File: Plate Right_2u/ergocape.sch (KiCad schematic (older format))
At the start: 42 parts

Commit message: cleanup and finish the case files
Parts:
- removed K_ESC1: KEYSW, acheron_SwitchSlots:slotMX100, symbol keyboard_parts:KEYSW
- added K_BKSP_1: KEYSW, usbc_footprint:slotMX200, symbol keyboard_parts:KEYSW
- H1, H10, H11, H12, H2, H3, H5, H6, H8, H9: footprint usbc_footprint:mount_hole_2.4x4 -> acheron_MountingHoles:MountingHole_2.5x4.0mm
- K_1, K_2, K_3, K_4, K_5, K_A1, K_ALT1, K_B1, K_BOT_1U_1, K_BOT_1U_2, K_C1, K_CTRL1, K_D1, K_E1, K_F1, K_G1, K_Q1, K_R1, K_S1, K_T1, K_TAB1, K_TH_1U_1, K_TH_1U_2, K_V1, K_W1, K_WIN1, K_X1, K_Z1: footprint acheron_SwitchSlots:slotMX100 -> usbc_footprint:slotMX100
- K_ENTER_rev_2.25u_1, K_SHIFT_REV_2.75_1, K_THUMB_2U1: footprint acheron_SwitchSlots:slotMX200 -> usbc_footprint:slotMX200
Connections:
- wire segments 5 -> 1

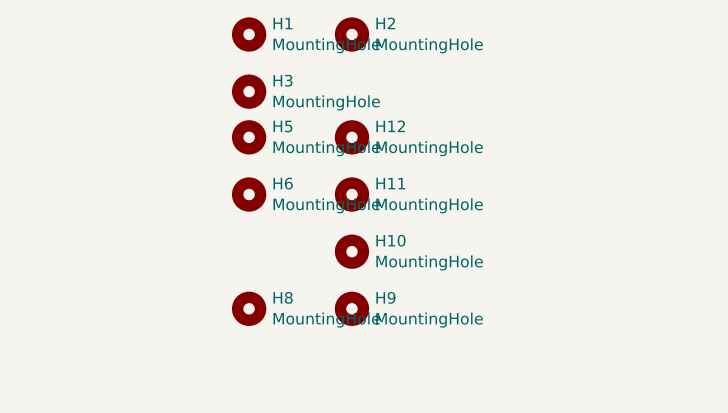
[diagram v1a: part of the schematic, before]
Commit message: finalize plate and mounting holes
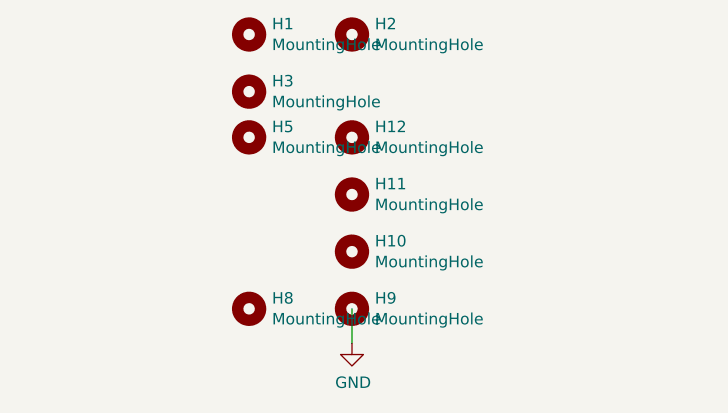
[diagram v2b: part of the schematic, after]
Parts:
- removed H6: MountingHole, acheron_MountingHoles:MountingHole_2.5x4.0mm, symbol Mechanical:MountingHole
- H1, H10, H11, H12, H2, H3, H5, H8, H9: footprint acheron_MountingHoles:MountingHole_2.5x4.0mm -> MountingHole:MountingHole_2.7mm_M2.5
- K_1, K_2, K_3, K_4, K_5, K_A1, K_ALT1, K_B1, K_BOT_1U_1, K_BOT_1U_2, K_C1, K_CTRL1, K_D1, K_E1, K_F1, K_G1, K_Q1, K_R1, K_S1, K_T1, K_TAB1, K_TH_1U_1, K_TH_1U_2, K_V1, K_W1, K_WIN1, K_X1, K_Z1: footprint usbc_footprint:slotMX100 -> usbc_footprint:1u_uni
- K_BKSP_1, K_ENTER_rev_2.25u_1, K_SHIFT_REV_2.75_1, K_THUMB_2U1: footprint usbc_footprint:slotMX200 -> usbc_footprint:mixed_2u_uni_centered
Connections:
- net labels added: GND
- wire segments 1 -> 2
